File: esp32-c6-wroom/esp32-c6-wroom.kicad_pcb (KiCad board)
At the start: 2 copper layers, 1 part, among them U1 ESP32-C6-WROOM-1-N8

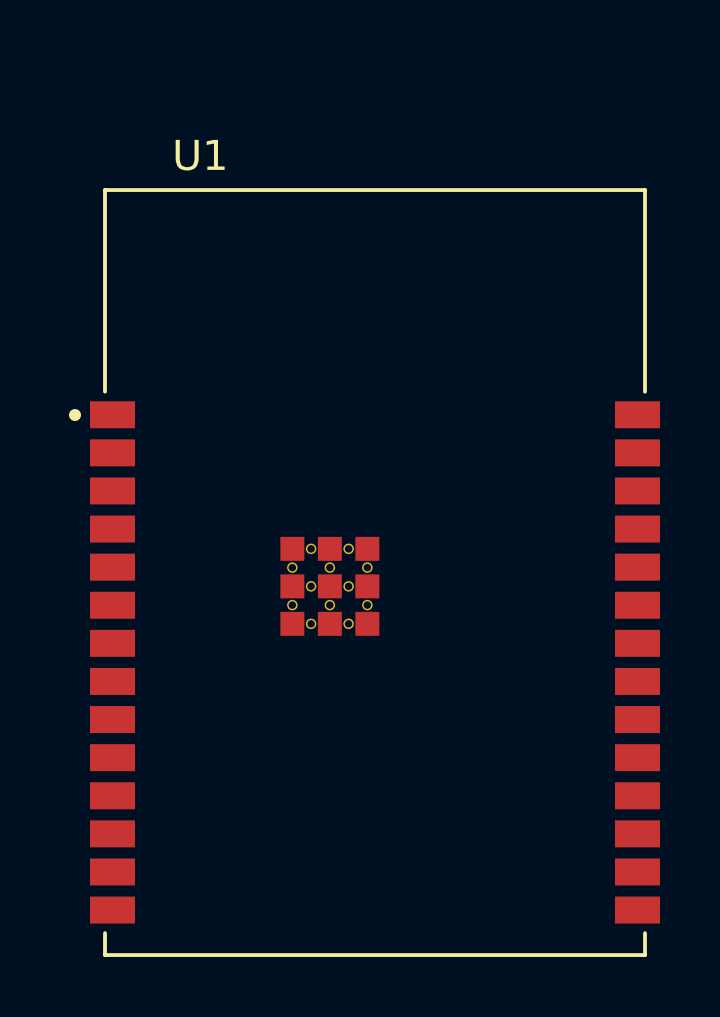
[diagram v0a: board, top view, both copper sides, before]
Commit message: fix: use official espressif lib for esp32-c6 projects
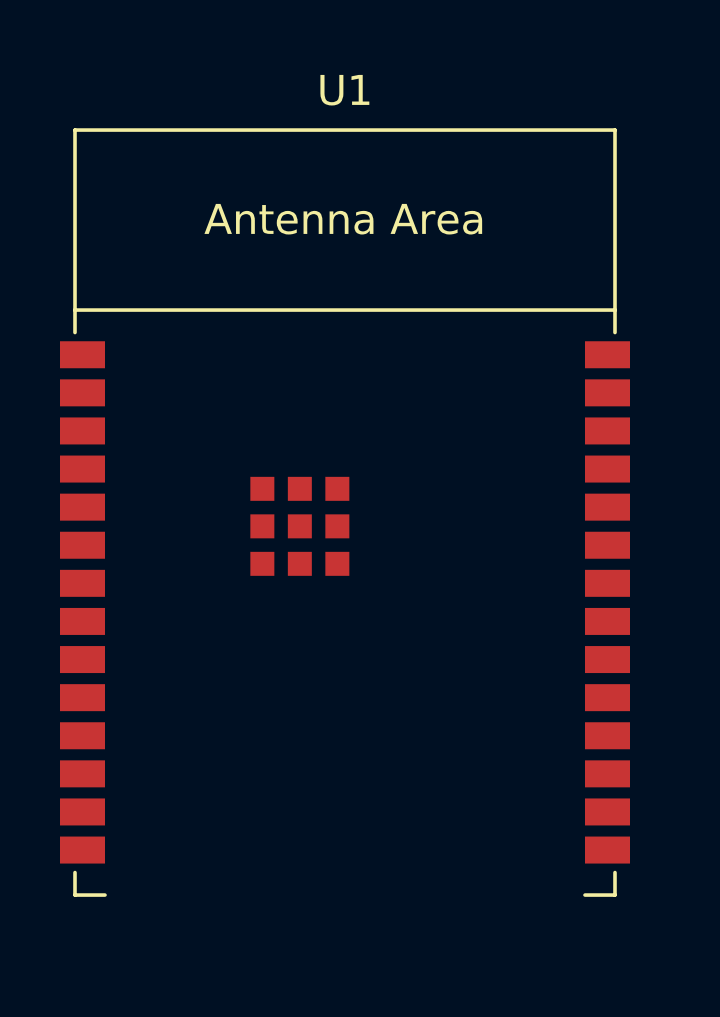
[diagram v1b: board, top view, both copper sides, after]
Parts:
- U1: value ESP32-C6-WROOM-1-N8 -> ESP32-C6-WROOM-1; footprint ESP32:XCVR_ESP32-C6-WROOM-1-N8 -> PCM_Espressif:ESP32-C6-WROOM-1
- moved U1 1.41 mm to (149.8, 100.2)
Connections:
- U1 pad 1: GND -> Net-(U1-GND-Pad1)
- U1 pad 28: GND -> Net-(U1-GND-Pad1)
